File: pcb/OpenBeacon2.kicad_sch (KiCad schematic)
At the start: 53 parts, among them J1 Bias V, J11 BNC, J16 SMA CLKIN, J2 PAI+, J3 PAI-, J6 SMA, J9 GND, Q1 2N7002, Q2 MMBT4403, Q3 BS170, Q8 BS170, U1 TLV61046A, U2 25.000 MHz TCXO, U3 SN74LVC1G17, U4 SI5351C-B-GMR, U5 MCP4725A1T-E/CH

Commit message: U2 TCXO pin 1 to GND per YXC datasheet (was OE tied to VDD via DNP R13): rename symbol pin, ground with continuous wire, delete R13. Vendor EtherkitKicadLibrary/Measurement_Points footprints and project symbol libs into pcb/lib with ${KIPRJMOD} paths; fp/sym-lib-table no longer reference /home/jason. ERC 0 errors
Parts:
- removed R13: 0, Resistor_SMD:R_0805_2012Metric, symbol EtherkitKicadLibrary:R
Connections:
- net GND: now also U2.1 (GND)
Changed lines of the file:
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@@
-	)
-	(symbol
-		(lib_id "EtherkitKicadLibrary:R")
-		(at 177.8 31.75 0)
-		(unit 1)
-		(body_style 1)
-		(exclude_from_sim no)
-		(in_bom yes)
-		(on_board yes)
-		(in_pos_files yes)
-		(dnp yes)
-		(property "Reference" "R13"
-			(at 174.625 30.48 0)
-			(effects
-				(font
-					(size 1.27 1.27)
-				)
-				(justify right)
-			)
-		)
-		(property "Value" "0"
-			(at 174.625 33.02 0)
-			(effects
-				(font
-					(size 1.27 1.27)
-				)
-				(justify right)
-			)
-		)
-		(property "Footprint" "Resistor_SMD:R_0805_2012Metric"
-			(at 177.8 31.75 0)
-			(effects
-				(font
-					(size 1.27 1.27)
-				)
-				(hide yes)
-			)
-		)
-		(property "Datasheet" ""
-			(at 177.8 31.75 0)
-			(effects
-				(font
-					(size 1.27 1.27)
-				)
-				(hide yes)
-			)
-		)
-		(property "MPN" "0805W8F0000T5E"
-			(at 177.8 31.75 0)
-			(effects
-				(font
-					(size 1.27 1.27)
-				)
-				(hide yes)
-			)
-		)
-		(property "Manufacturer" "UNI-ROYAL(Uniroyal Elec)"
-			(at 177.8 31.75 0)
-			(effects
-				(font
-					(size 1.27 1.27)
-				)
-				(hide yes)
-			)
-		)
-		(property "LCSC" "C17477"
-			(at 177.8 31.75 0)
-			(effects
-				(font
-					(size 1.27 1.27)
-				)
-				(hide yes)
-			)
-		)
-		(pin "1"
-		)
-		(pin "2"
-		)
-		(instances
-			(project "OpenBeacon2"
-				(path "/046319a3-a6ce-4e59-a888-94e340127381"
-					(reference "R13")
-					(unit 1)
-				)
-			)
-		)
 	)
 	(symbol
@@
 		)
 	)
+	(symbol
+		(lib_id "OpenBeacon2-rescue:GND-OpenBeaconMini-rescue")
+		(at 177.8 38.1 0)
+		(unit 1)
+		(body_style 1)
+		(exclude_from_sim no)
+		(in_bom yes)
+		(on_board yes)
+		(in_pos_files yes)
+		(dnp no)
+		(property "Reference" "#PWR0400"
+			(at 177.8 44.45 0)
+			(hide yes)
+			(show_name no)
+			(do_not_autoplace no)
+			(effects
+				(font
+					(size 1.27 1.27)
+				)
+			)
+		)
+		(property "Value" "GND"
+			(at 180.467 39.497 0)
+			(show_name no)
+			(do_not_autoplace no)
+			(effects
+				(font
+					(size 0.762 0.762)
+				)
+			)
+		)
+		(property "Footprint" ""
+			(at 177.8 38.1 0)
+			(hide yes)
+			(show_name no)
+			(do_not_autoplace no)
+			(effects
+				(font
+					(size 1.27 1.27)
+				)
+			)
+		)
+		(property "Datasheet" ""
+			(at 177.8 38.1 0)
+			(hide yes)
+			(show_name no)
+			(do_not_autoplace no)
+			(effects
+				(font
+					(size 1.27 1.27)
+				)
+			)
+		)
+		(property "Description" ""
+			(at 177.8 38.1 0)
+			(show_name no)
+			(do_not_autoplace no)
+			(effects
+				(font
+					(size 1.27 1.27)
+				)
+			)
+		)
+		(pin "1"
+		)
+		(instances
+			(project "OpenBeacon2"
+				(path "/046319a3-a6ce-4e59-a888-94e340127381"
+					(reference "#PWR0400")
+					(unit 1)
+				)
+			)
+		)
+	)
+	(wire
+		(pts
+			(xy 177.8 35.56) (xy 177.8 38.1)
+		)
+		(stroke
+			(width 0)
+			(type default)
+		)
+	)

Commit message: BOM: fill MPN/Manufacturer/LCSC for 47 Rev B parts (Basic preferred; C3 10u/25V, C7 1u/50V, C11 100n/50V). Hand-solder parts J11, Q3, Q8, DS1, L2 marked Assembly=hand solder and excluded from pos files. Nets unchanged, ERC 0 errors
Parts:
- C1, C10, C11, C14, C5, C6, C8: LCSC (none) -> C49678; MPN (none) -> CC0805KRX7R9BB104; Manufacturer (none) -> YAGEO
- C2: LCSC (none) -> C1779; MPN (none) -> CL21A475KAQNNNE; Manufacturer (none) -> Samsung Electro-Mechanics
- C3: LCSC (none) -> C15850; MPN (none) -> CL21A106KAYNNNE; Manufacturer (none) -> Samsung Electro-Mechanics
- C4: LCSC (none) -> C1710; MPN (none) -> CL21B103KBANNNC; Manufacturer (none) -> Samsung Electro-Mechanics
- C7, C9: LCSC (none) -> C28323; MPN (none) -> CL21B105KBFNNNE; Manufacturer (none) -> Samsung Electro-Mechanics
- J11: Assembly (none) -> Hand solder - exclude from JLC assembly; LCSC (none) -> C6956217
- L1: LCSC (none) -> C1329533; MPN (none) -> FDSD0420-H-100M=P3; Manufacturer (none) -> Murata Electronics
- L2: Assembly (none) -> Hand solder - exclude from JLC assembly; LCSC (none) -> C6078003; MPN (none) -> 2843002402; Manufacturer (none) -> Fair-Rite Products
- Q1: LCSC (none) -> C8545; MPN (none) -> 2N7002; Manufacturer (none) -> Jiangsu Changjing Electronics Technology
- Q2: LCSC (none) -> C8513; MPN (none) -> MMBT4403; Manufacturer (none) -> Jiangsu Changjing Electronics Technology
- Q3, Q8: Assembly (none) -> Hand solder - exclude from JLC assembly; LCSC (none) -> C111691
- R1, R2, R3: LCSC (none) -> C17560; MPN (none) -> 0805W8F2202T5E; Manufacturer (none) -> UNI-ROYAL(Uniroyal Elec)
- R5: LCSC (none) -> C26010; MPN (none) -> 0805W8F3301T5E; Manufacturer (none) -> UNI-ROYAL(Uniroyal Elec)
- R6: LCSC (none) -> C17415; MPN (none) -> 0805W8F100JT5E; Manufacturer (none) -> UNI-ROYAL(Uniroyal Elec)
- R7: LCSC (none) -> C17757; MPN (none) -> 0805W8F560JT5E; Manufacturer (none) -> UNI-ROYAL(Uniroyal Elec)
- R8: LCSC (none) -> C25271; MPN (none) -> 0805W8F100KT5E; Manufacturer (none) -> UNI-ROYAL(Uniroyal Elec)
- U1: LCSC (none) -> C464815; MPN (none) -> TLV61046ADBVR; Manufacturer (none) -> Texas Instruments
- U3: LCSC (none) -> C7836; MPN (none) -> SN74LVC1G17DBVR; Manufacturer (none) -> Texas Instruments
- U5: LCSC (none) -> C61423; MPN (none) -> MCP4725A1T-E/CH; Manufacturer (none) -> Microchip Technology

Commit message: Exclude bare test pads J1, J2, J3, J9 from BOM
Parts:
- J1, J2, J3, J9: now left out of the parts list
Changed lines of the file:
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@@
 		(body_style 1)
 		(exclude_from_sim no)
-		(in_bom yes)
+		(in_bom no)
 		(on_board yes)
 		(in_pos_files yes)
@@
 		(body_style 1)
 		(exclude_from_sim no)
-		(in_bom yes)
+		(in_bom no)
 		(on_board yes)
 		(in_pos_files yes)
@@
 		(body_style 1)
 		(exclude_from_sim no)
-		(in_bom yes)
+		(in_bom no)
 		(on_board yes)
 		(in_pos_files yes)
@@
 		(body_style 1)
 		(exclude_from_sim no)
-		(in_bom yes)
-		(on_board yes)
-		(in_pos_files yes)
+		(in_bom no)
+		(on_board yes)
+		(in_pos_files yes)

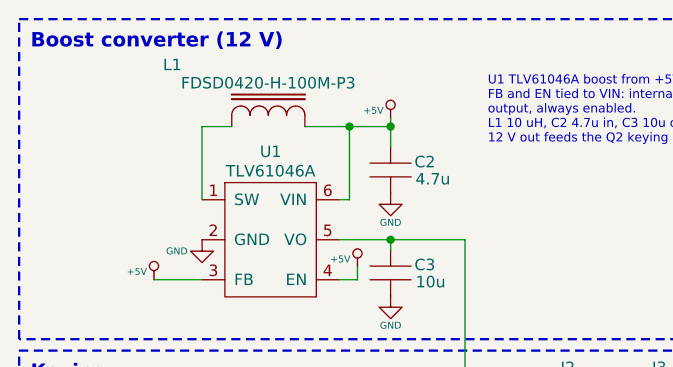
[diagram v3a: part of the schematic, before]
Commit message: LPF F2-F5: hand-wound T30 toroid design (1 W max); L1/C3 part swaps
- Move F2-F5 to new nested A4 sheet "LPF Filters" (lpf_filters.kicad_sch),
  instantiated from Filter Bank; same F*_IN/F*_OUT nets to the relay tree.
- 12 inductors -> hand-wound Micrometals T30-2 (F2/F3) / T30-6 (F4/F5),
  values/turns/wire per ob2_filters/t30 design. Fields: Core, Turns, Wire,
  MPN=T30-x, Supplier=Kits and Parts. DNP, excluded from pos files, no LCSC.
  Footprint Inductor_THT:L_Toroid_Vertical_L10.0mm_W5.0mm_P5.08mm.
- All filter caps 0603 C0G/NP0 50 V JLC Basic/preferred, parallel combos
  as designed (C208+ etc.). C406/C407/C507 kept (still used; C407 now fitted).
- Winding table + notes on the LPF sheet.
- L1 -> Sunlord MWSA0402S-100MT (C408339), existing Murata100M pads fit.
- C3 -> Samsung CL31A106KBHNNNE (C13585), 1206 footprint.
- ERC 0 errors; netlist matches simulated topology node for node.
- Regenerate docs/OpenBeacon2_schematic.pdf.
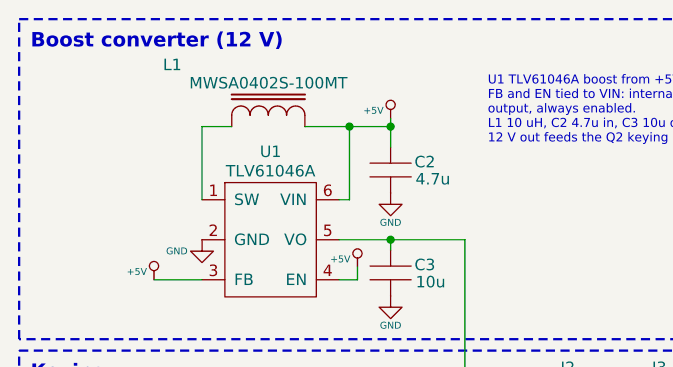
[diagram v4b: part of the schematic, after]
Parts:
- C3: footprint Capacitor_SMD:C_0805_2012Metric -> Capacitor_SMD:C_1206_3216Metric; LCSC C15850 -> C13585; MPN CL21A106KAYNNNE -> CL31A106KBHNNNE
- L1: value FDSD0420-H-100M-P3 -> MWSA0402S-100MT; LCSC C1329533 -> C408339; MPN FDSD0420-H-100M=P3 -> MWSA0402S-100MT; Manufacturer Murata Electronics -> Sunlord
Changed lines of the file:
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@@
 			)
 		)
-		(property "Value" "FDSD0420-H-100M-P3"
+		(property "Value" "MWSA0402S-100MT"
 			(at 41.656 21.082 90)
 			(show_name no)
@@
 			)
 		)
-		(property "MPN" "FDSD0420-H-100M=P3"
+		(property "MPN" "MWSA0402S-100MT"
 			(at 30.988 19.05 90)
 			(effects
@@
 			)
 		)
-		(property "Manufacturer" "Murata Electronics"
+		(property "Manufacturer" "Sunlord"
 			(at 30.988 19.05 90)
 			(effects
@@
 			)
 		)
-		(property "LCSC" "C1329533"
+		(property "LCSC" "C408339"
 			(at 30.988 19.05 90)
 			(effects
@@
 			)
 		)
-		(property "Footprint" "Capacitor_SMD:C_0805_2012Metric"
+		(property "Footprint" "Capacitor_SMD:C_1206_3216Metric"
 			(at 55.245 42.164 0)
 			(hide yes)
@@
 			)
 		)
-		(property "MPN" "CL21A106KAYNNNE"
+		(property "MPN" "CL31A106KBHNNNE"
 			(at 59.055 41.275 0)
 			(effects
@@
 			)
 		)
-		(property "LCSC" "C15850"
+		(property "LCSC" "C13585"
 			(at 59.055 41.275 0)
 			(effects

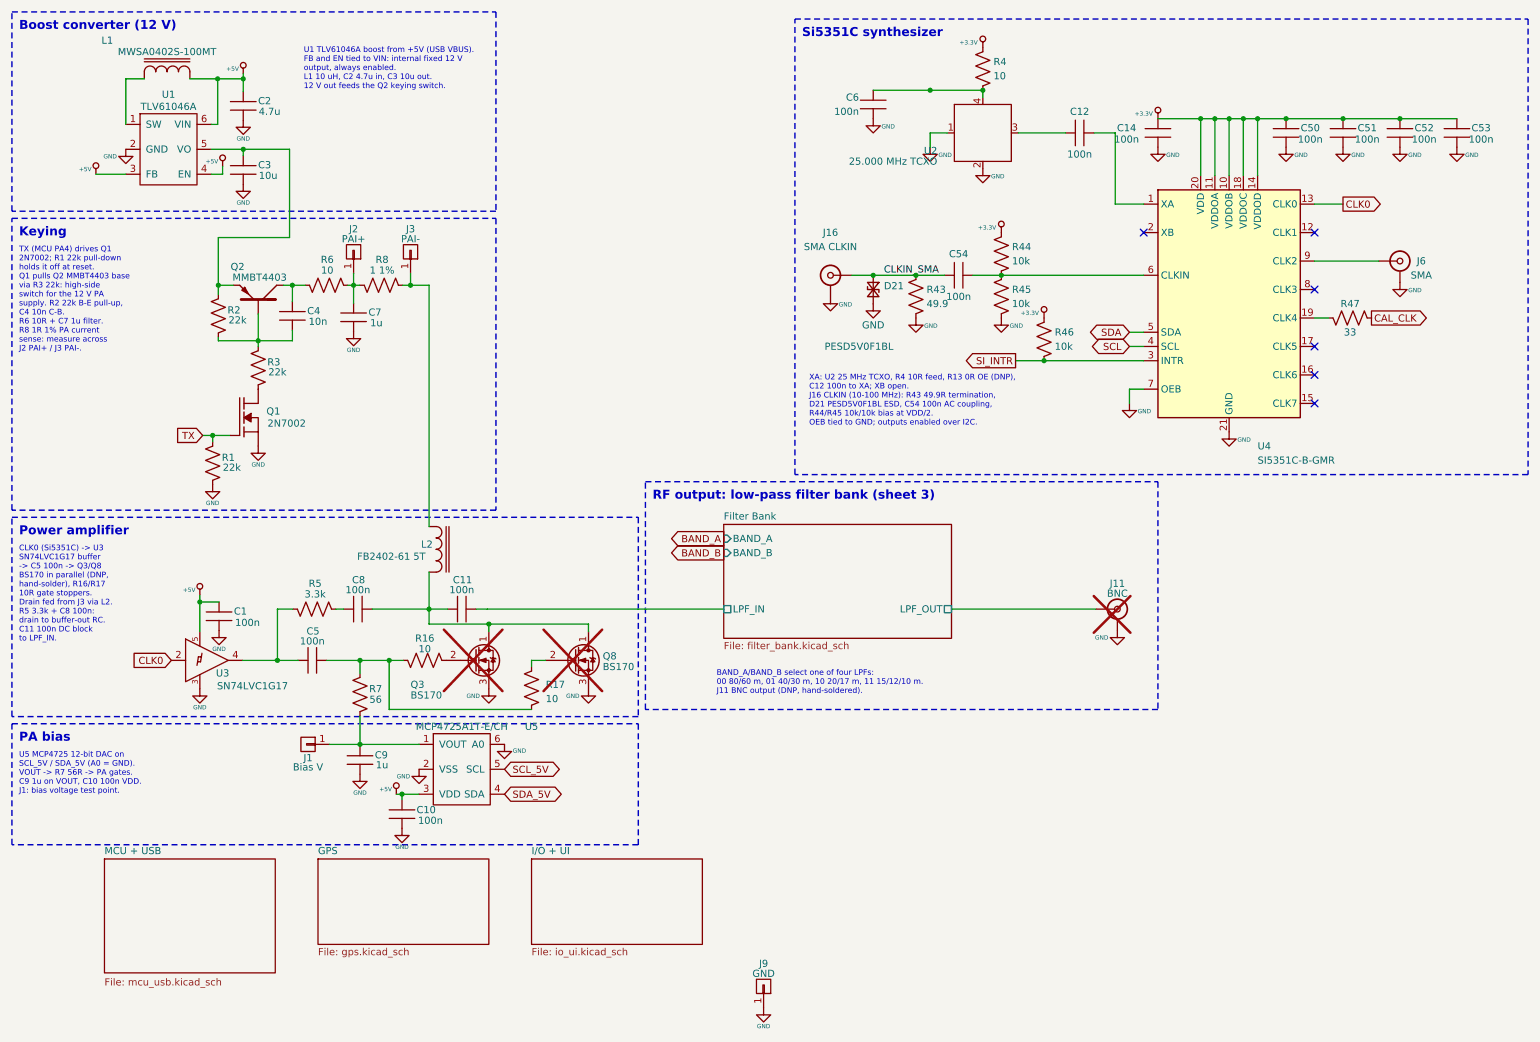
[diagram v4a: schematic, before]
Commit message: Rev C layout: board grown to 130x110 mm, headers J4/J5/J8/J10/J14 removed, power rework layout
- Outline grown 10 mm on top and left edges (130x110 mm); locked edge parts moved with outline
- Removed J4, J5, J8, J10, J14 and support parts (D13-D15, D17, D19, D20, R64-R67, R69-R71, R75-R79); UPDI J13 kept
- Power rework placed and routed (TPS61085 boost, INA193 U14, Q10 soft-start)
- Y1 placed at U9, stray passives moved, silkscreen labels cleaned up
- Routed: DRC 0 errors / 0 unconnected, schematic parity 0, ERC 0; layout gate 11/11
- DRU: ESC_* fine-pitch escape 0.20 mm rule areas, U1 pad-to-pad 0.14 mm
- In2 keep-away waivers (GND-plane shielded): Q2 drain, MCU_TX, MCU_RX near R6, 22.6 mm MCU_RX run near U9
- Libs: 6x6 H13 switch, OLED pin-header module footprint, updated symbols
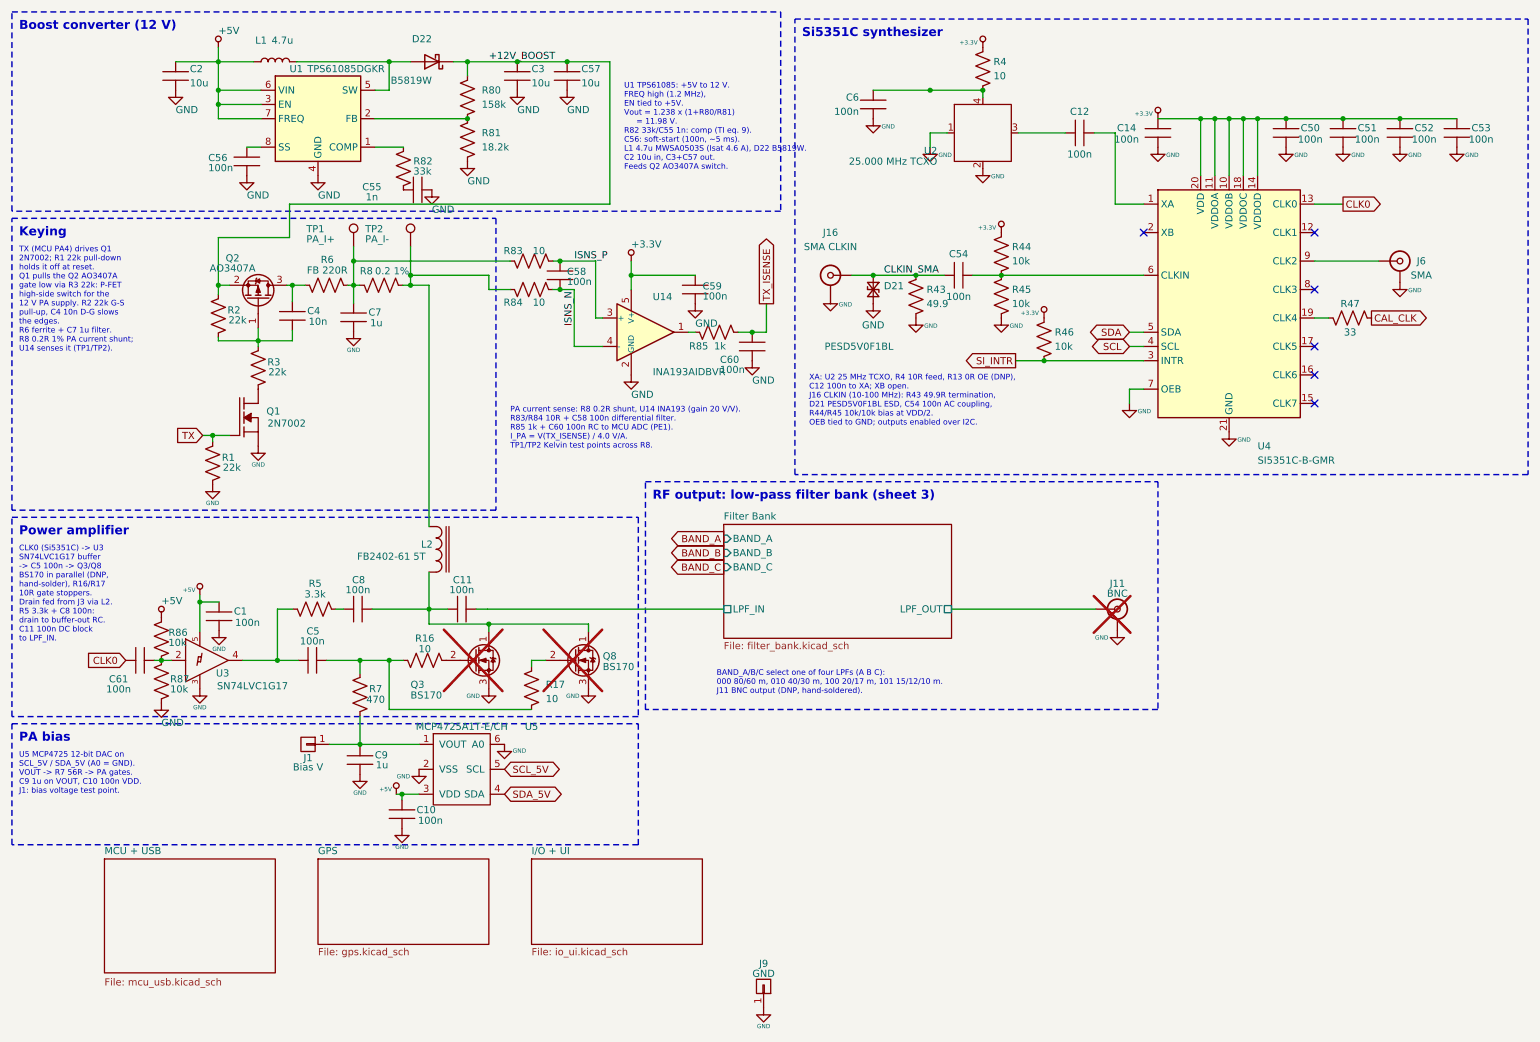
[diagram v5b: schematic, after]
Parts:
- removed J2: PAI+, Measurement_Points:Measurement_Point_Square-TH_Small, symbol EtherkitKicadLibrary:CONN_01X01
- removed J3: PAI-, Measurement_Points:Measurement_Point_Square-TH_Small, symbol EtherkitKicadLibrary:CONN_01X01
- removed L1: MWSA0402S-100MT, EtherkitKicadLibrary:Murata100M, symbol EtherkitKicadLibrary:L-IRONCORE
- removed Q2: MMBT4403, EtherkitKicadLibrary:SOT23-MMBT440X, symbol EtherkitKicadLibrary:PNP
- removed U1: TLV61046A, EtherkitKicadLibrary:SOT23-6, symbol EtherkitKicadLibrary:TLV61046A
- added C55: 1n, Capacitor_SMD:C_0603_1608Metric, symbol EtherkitKicadLibrary:C
- added C56, C58, C59, C60, C61: 100n, Capacitor_SMD:C_0603_1608Metric, symbol EtherkitKicadLibrary:C
- added C57: 10u, Capacitor_SMD:C_1206_3216Metric, symbol EtherkitKicadLibrary:C
- added D22: B5819W, Diode_SMD:D_SOD-123, symbol OpenBeacon2:D_Schottky
- added L1: 4.7u, Inductor_SMD:L_Sunlord_MWSA0503S, symbol OpenBeacon2:L
- added Q2: AO3407A, EtherkitKicadLibrary:SOT23-MMBT440X, symbol OpenBeacon2:AO3407A
- added R80: 158k, Resistor_SMD:R_0603_1608Metric, symbol EtherkitKicadLibrary:R
- added R81: 18.2k, Resistor_SMD:R_0603_1608Metric, symbol EtherkitKicadLibrary:R
- added R82: 33k, Resistor_SMD:R_0603_1608Metric, symbol EtherkitKicadLibrary:R
- added R83, R84: 10, Resistor_SMD:R_0603_1608Metric, symbol EtherkitKicadLibrary:R
- added R85: 1k, Resistor_SMD:R_0603_1608Metric, symbol EtherkitKicadLibrary:R
- added R86, R87: 10k, Resistor_SMD:R_0603_1608Metric, symbol EtherkitKicadLibrary:R
- added TP1: PA_I+, Measurement_Points:Measurement_Point_Square-TH_Small, symbol OpenBeacon2:TestPoint
- added TP2: PA_I-, Measurement_Points:Measurement_Point_Square-TH_Small, symbol OpenBeacon2:TestPoint
- added U1: TPS61085DGKR, Package_SO:VSSOP-8_3x3mm_P0.65mm, symbol OpenBeacon2:TPS61085DGK
- added U14: INA193AIDBVR, Package_TO_SOT_SMD:SOT-23-5, symbol OpenBeacon2:INA193
- C14: footprint Capacitor_SMD:C_0805_2012Metric -> Capacitor_SMD:C_0402_1005Metric; LCSC C49678 -> C1525; MPN CC0805KRX7R9BB104 -> CL05B104KO5NNNC; Manufacturer YAGEO -> Samsung Electro-Mechanics
- C2: value 4.7u -> 10u; LCSC C1779 -> C15850; MPN CL21A475KAQNNNE -> CL21A106KAYNNNE
- R6: value 10 -> FB 220R; footprint Resistor_SMD:R_0805_2012Metric -> Inductor_SMD:L_0603_1608Metric; LCSC C17415 -> C80165; MPN 0805W8F100JT5E -> BLM18PG221SN1D; Manufacturer UNI-ROYAL(Uniroyal Elec) -> Murata Electronics
- R7: value 56 -> 470; LCSC C17757 -> C17710; MPN 0805W8F560JT5E -> 0805W8F4700T5E
- R8: value 1 1% -> 0.2 1%; LCSC C25271 -> C44051; MPN 0805W8F100KT5E -> 0805W8F200LT5E
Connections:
- net +3.3V: now also C59.1, U14.5 (V+)
- net +5V: now also L1.1, R86.1, U1.3 (EN), U1.6 (VIN), U1.7 (FREQ)
- net CLK0: now also C61.1; no longer U3.2
- net GND: now also C55.2, C56.2, C57.2, C59.2, C60.2, R81.2, R87.2, U1.4 (GND), U14.2 (GND)
- net at L2.1, R8.1: now also R84.1, TP2.1
- net +12V_BOOST: now reaches C3.1, R2.1
- net +12V_BOOST: now also C57.1, D22.1 (K), Q2.2 (S), R80.1
- net at C4.2, R2.2, R3.1: now also Q2.1 (G)
- net at C4.1, R6.2: now also Q2.3 (D)
- net at C7.1, R6.1, R8.2: now also R83.1, TP1.1
- new net: C61.2, R86.2, R87.1, U3.2
- new net: R82.1, U1.1 (COMP)
- new net: C55.1, R82.2
- new net: C56.1, U1.8 (SS)
- new net: R85.1, U14.1
- new net: R80.2, R81.1, U1.2 (FB)
- new net: D22.2 (A), L1.2, U1.5 (SW)
- new net ISNS_N: C58.2, R84.2, U14.4 (-)
- new net ISNS_P: C58.1, R83.2, U14.3 (+)
- new net TX_ISENSE: C60.1, R85.2
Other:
- sheet Filter Bank ports: added BAND_C; removed none
- note added: "BAND_A/B/C select one of four LPFs (A B C): 000 80/60 m, 010 40/30 m, 100 20/17 m, 101 15/12/10 m. J11 BNC output (DNP, hand-soldered)."
- note added: "PA current sense: R8 0.2R shunt, U14 INA193 (gain 20 V/V). R83/R84 10R + C58 100n differential filter. R85 1k + C60 100n RC to MCU ADC (PE1). I_PA = V(TX_ISENSE) / 4.0 V/A. TP1/TP2 Kelvin test points across R8."
- note added: "TX (MCU PA4) drives Q1 2N7002; R1 22k pull-down holds it off at reset. Q1 pulls the Q2 AO3407A gate low via R3 22k: P-FET high-side switch for the 12 V PA supply. R2 22k G-S pull-up, C4 10n D-G slows the edges. R6 ferrite + C7 1u filter. R8 0.2R 1% PA current shunt; U14 senses it (TP1/TP2)."
- note added: "U1 TPS61085: +5V to 12 V. FREQ high (1.2 MHz), EN tied to +5V. Vout = 1.238 x (1+R80/R81) = 11.98 V. R82 33k/C55 1n: comp (TI eq. 9). C56: soft-start (100n, ~5 ms). L1 4.7u MWSA0503S (Isat 4.6 A), D22 B5819W. C2 10u in, C3+C57 out. Feeds Q2 AO3407A switch."
- note removed: "BAND_A/BAND_B select one of four LPFs: 00 80/60 m, 01 40/30 m, 10 20/17 m, 11 15/12/10 m. J11 BNC output (DNP, hand-soldered)."
- note removed: "TX (MCU PA4) drives Q1 2N7002; R1 22k pull-down holds it off at reset. Q1 pulls Q2 MMBT4403 base via R3 22k: high-side switch for the 12 V PA supply. R2 22k B-E pull-up, C4 10n C-B. R6 10R + C7 1u filter. R8 1R 1% PA current sense: measure across J2 PAI+ / J3 PAI-."
- note removed: "U1 TLV61046A boost from +5V (USB VBUS). FB and EN tied to VIN: internal fixed 12 V output, always enabled. L1 10 uH, C2 4.7u in, C3 10u out. 12 V out feeds the Q2 keying switch."

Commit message: Renumber all references monotonically 1..N per prefix; sync PCB silk labels and auto-named nets; ERC 0, DRC 0/0
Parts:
- renumbered C2 to C1, C53 to C10, C56 to C11, C55 to C12, C58 to C13, C54 to C14, C59 to C15, C4 to C16, C7 to C17, C60 to C18, C8 to C19, C3 to C2, C11 to C20, C1 to C21, C61 to C22, C5 to C23, C9 to C24, C10 to C25, C57 to C3, C6 to C4, C12 to C5, C14 to C6, C50 to C7, C51 to C8, C52 to C9, D22 to D1, D21 to D2, J6 to J1, J16 to J2, J11 to J3, J1 to J4, J9 to J5, Q2 to Q1, Q1 to Q2, Q8 to Q4, R4 to R1, R43 to R10, R45 to R11, R2 to R12, R47 to R13, R85 to R14, R46 to R15, R3 to R16, R1 to R17, R5 to R18, R86 to R19, R80 to R2, R16 to R20, R87 to R21, R17 to R22, R7 to R23, R81 to R3, R82 to R4, R44 to R5, R83 to R6, R6 to R7, R84 to R9, U4 to U3, U14 to U4, U3 to U5, U5 to U6
